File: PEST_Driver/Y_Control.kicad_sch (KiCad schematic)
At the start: 72 parts, among them J1 Conn_01x02, J2 Conn_01x02, J3 Conn_01x02, J4 Conn_01x02, J5 Conn_01x02, J6 Conn_01x02, J7 Conn_01x02, J8 Conn_01x02, U19 74HC4051, U2 74HC4051, U20 74HC4051, U21 74HC595, U22 74HC4051, U3 74HC4051

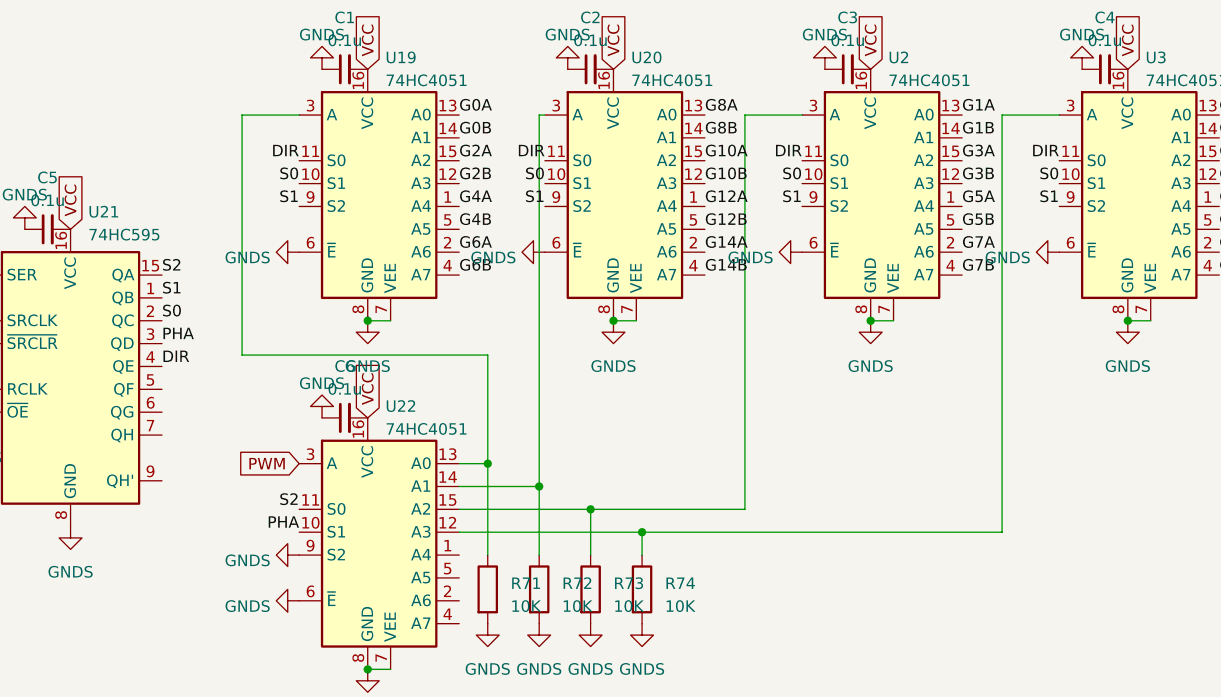
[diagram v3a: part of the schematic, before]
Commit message: Created basic DRIFT bus schematic and fixed PEST driver numbering
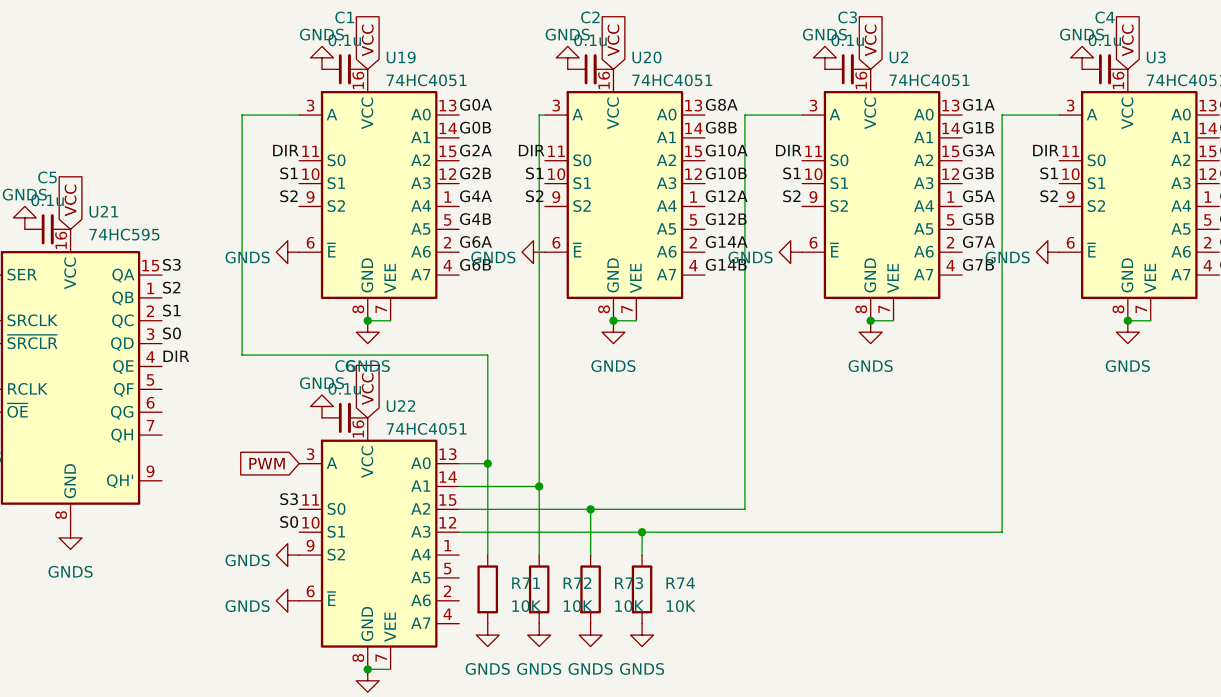
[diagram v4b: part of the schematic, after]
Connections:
- net PHA is gone; now on net S0: U21.3 (QD), U22.10 (S1)
- net S0: no longer U19.10 (S1), U2.10 (S1), U20.10 (S1), U21.2 (QC), U3.10 (S1)
- net S1: now also U19.10 (S1), U2.10 (S1), U20.10 (S1), U21.2 (QC), U3.10 (S1); no longer U19.9 (S2), U2.9 (S2), U20.9 (S2), U21.1 (QB), U3.9 (S2)
- net S2: now also U19.9 (S2), U2.9 (S2), U20.9 (S2), U21.1 (QB), U3.9 (S2); no longer U21.15 (QA), U22.11 (S0)
- new net S3: U21.15 (QA), U22.11 (S0)
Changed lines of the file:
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@@
     (effects (font (size 1.27 1.27)) (justify left bottom))
   )
-  (label "S0" (at 120.65 104.14 180) (fields_autoplaced)
+  (label "S1" (at 120.65 104.14 180) (fields_autoplaced)
     (effects (font (size 1.27 1.27)) (justify right bottom))
   )
@@
     (effects (font (size 1.27 1.27)) (justify left bottom))
   )
-  (label "S1" (at 149.225 106.68 180) (fields_autoplaced)
+  (label "S2" (at 149.225 106.68 180) (fields_autoplaced)
     (effects (font (size 1.27 1.27)) (justify right bottom))
   )
@@
     (effects (font (size 1.27 1.27)) (justify left bottom))
   )
-  (label "S0" (at 149.225 104.14 180) (fields_autoplaced)
-    (effects (font (size 1.27 1.27)) (justify right bottom))
-  )
-  (label "S0" (at 92.075 104.14 180) (fields_autoplaced)
+  (label "S1" (at 149.225 104.14 180) (fields_autoplaced)
+    (effects (font (size 1.27 1.27)) (justify right bottom))
+  )
+  (label "S1" (at 92.075 104.14 180) (fields_autoplaced)
     (effects (font (size 1.27 1.27)) (justify right bottom))
   )
@@
     (effects (font (size 1.27 1.27)) (justify left bottom))
   )
-  (label "S1" (at 49.53 116.84 0) (fields_autoplaced)
+  (label "S2" (at 49.53 116.84 0) (fields_autoplaced)
     (effects (font (size 1.27 1.27)) (justify left bottom))
   )
@@
     (effects (font (size 1.27 1.27)) (justify right bottom))
   )
-  (label "S0" (at 64.77 104.14 180) (fields_autoplaced)
+  (label "S1" (at 64.77 104.14 180) (fields_autoplaced)
     (effects (font (size 1.27 1.27)) (justify right bottom))
   )
@@
     (effects (font (size 1.27 1.27)) (justify right bottom))
   )
-  (label "S2" (at 64.77 140.335 180) (fields_autoplaced)
+  (label "S3" (at 64.77 140.335 180) (fields_autoplaced)
     (effects (font (size 1.27 1.27)) (justify right bottom))
   )
@@
     (effects (font (size 1.27 1.27)) (justify left bottom))
   )
-  (label "PHA" (at 64.77 142.875 180) (fields_autoplaced)
+  (label "S0" (at 64.77 142.875 180) (fields_autoplaced)
     (effects (font (size 1.27 1.27)) (justify right bottom))
   )
@@
     (effects (font (size 1.27 1.27)) (justify left bottom))
   )
-  (label "S1" (at 92.075 106.68 180) (fields_autoplaced)
+  (label "S2" (at 92.075 106.68 180) (fields_autoplaced)
     (effects (font (size 1.27 1.27)) (justify right bottom))
   )
@@
     (effects (font (size 1.27 1.27)) (justify right bottom))
   )
-  (label "S0" (at 49.53 119.38 0) (fields_autoplaced)
+  (label "S1" (at 49.53 119.38 0) (fields_autoplaced)
     (effects (font (size 1.27 1.27)) (justify left bottom))
   )
@@
     (effects (font (size 1.27 1.27)) (justify left bottom))
   )
-  (label "S2" (at 49.53 114.3 0) (fields_autoplaced)
+  (label "S3" (at 49.53 114.3 0) (fields_autoplaced)
     (effects (font (size 1.27 1.27)) (justify left bottom))
   )
@@
     (effects (font (size 1.27 1.27)) (justify left bottom))
   )
-  (label "S1" (at 64.77 106.68 180) (fields_autoplaced)
+  (label "S2" (at 64.77 106.68 180) (fields_autoplaced)
     (effects (font (size 1.27 1.27)) (justify right bottom))
   )
@@
     (effects (font (size 1.27 1.27)) (justify left bottom))
   )
-  (label "PHA" (at 49.53 121.92 0) (fields_autoplaced)
+  (label "S0" (at 49.53 121.92 0) (fields_autoplaced)
     (effects (font (size 1.27 1.27)) (justify left bottom))
   )
@@
     (effects (font (size 1.27 1.27)) (justify left bottom))
   )
-  (label "S1" (at 120.65 106.68 180) (fields_autoplaced)
-    (effects (font (size 1.27 1.27)) (justify right bottom))
-  )
+  (label "S2" (at 120.65 106.68 180) (fields_autoplaced)
+    (effects (font (size 1.27 1.27)) (justify right bottom))
+  )
